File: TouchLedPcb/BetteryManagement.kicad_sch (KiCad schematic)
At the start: 1 part, among them U1 BQ25606

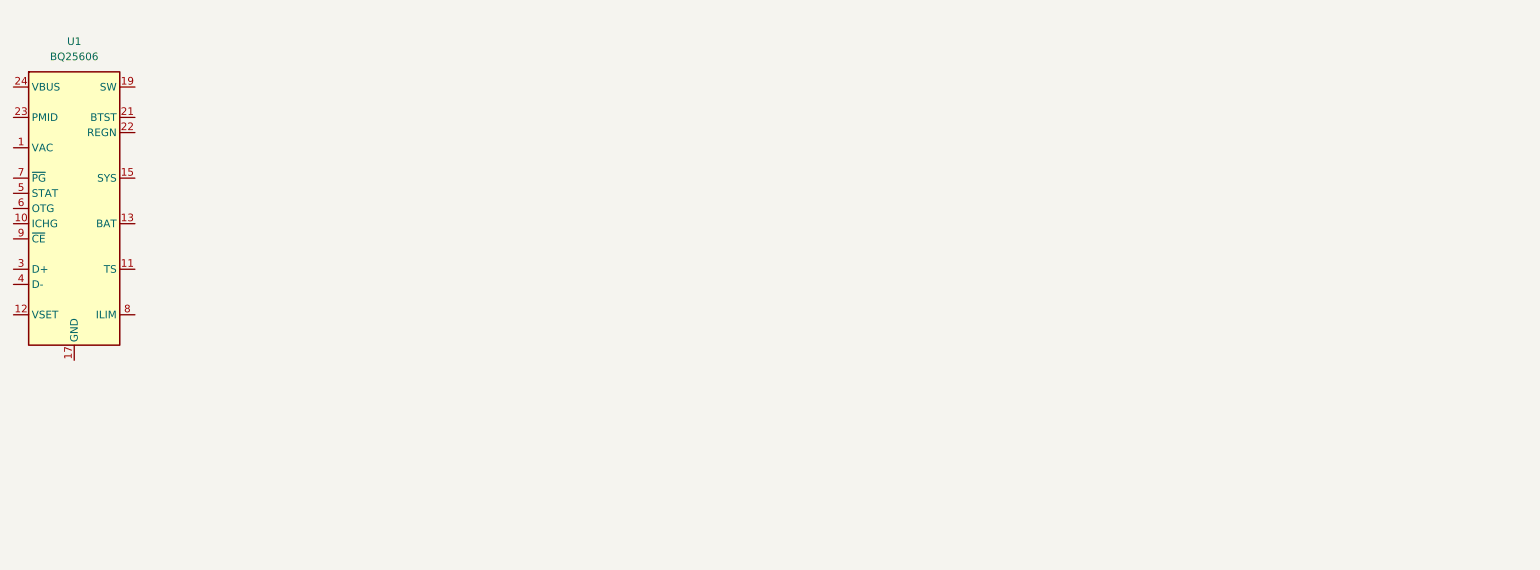
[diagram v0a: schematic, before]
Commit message: add excel for NTC 10k b=3950 calculation for BQ25606 -10~45C operation
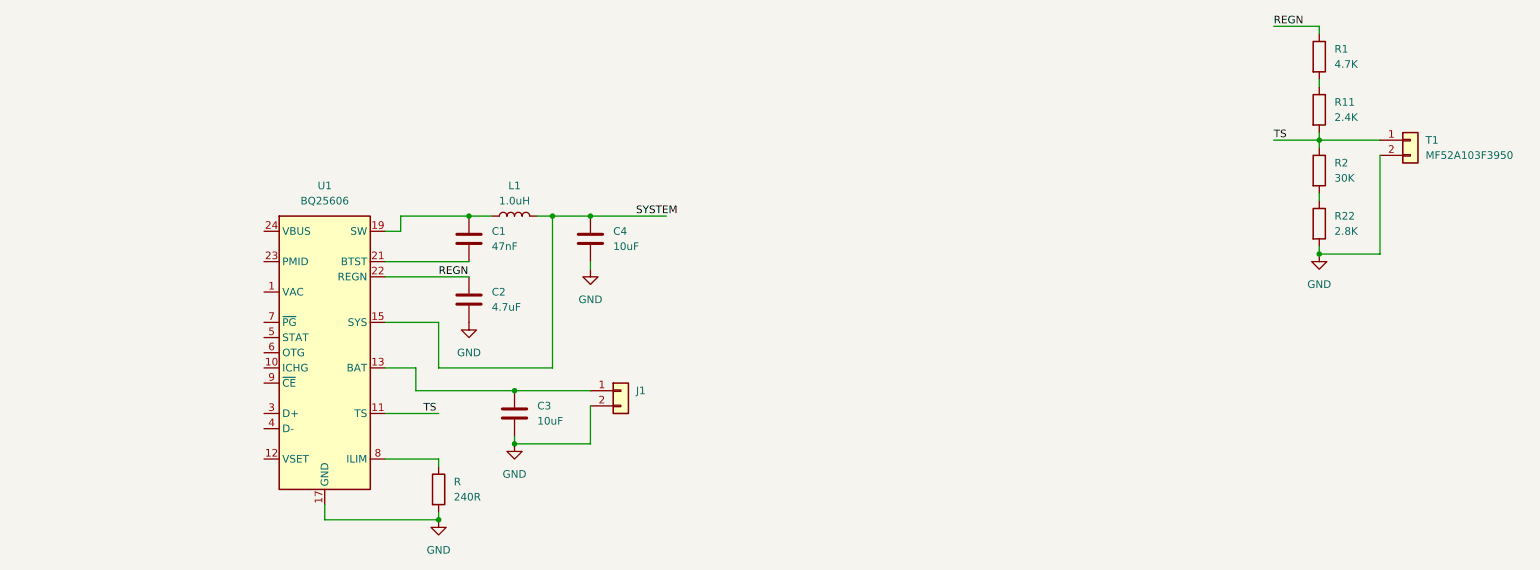
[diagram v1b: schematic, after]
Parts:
- added C1: 47nF, Capacitor_SMD:C_0805_2012Metric, symbol Device:C
- added C2: 4.7uF, Capacitor_SMD:C_1206_3216Metric, symbol Device:C
- added C3, C4: 10uF, Capacitor_SMD:C_0805_2012Metric, symbol Device:C
- added J1: ~, Connector_PinHeader_2.54mm:PinHeader_1x02_P2.54mm_Vertical, symbol Connector_Generic:Conn_01x02
- added L1: 1.0uH, Inductor_SMD:L_Chilisin_BMRA00050530, symbol Device:L
- added R: 240R, Resistor_SMD:R_0805_2012Metric, symbol Device:R
- added R1: 4.7K, Resistor_SMD:R_0805_2012Metric_Pad1.20x1.40mm_HandSolder, symbol Device:R
- added R11: 2.4K, Resistor_SMD:R_0805_2012Metric_Pad1.20x1.40mm_HandSolder, symbol Device:R
- added R2: 30K, Resistor_SMD:R_0805_2012Metric_Pad1.20x1.40mm_HandSolder, symbol Device:R
- added R22: 2.8K, Resistor_SMD:R_0805_2012Metric_Pad1.20x1.40mm_HandSolder, symbol Device:R
- added T1: MF52A103F3950, Connector_PinHeader_2.00mm:PinHeader_1x02_P2.00mm_Vertical, symbol Connector_Generic:Conn_01x02
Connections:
- net TS: now reaches U1.11 (TS)
- net TS: now also R11.2, R2.1, T1.1 (Pin_1)
- net at U1.13 (BAT), U1.14 (BAT): now also C3.1, J1.1 (Pin_1)
- net SYSTEM: now reaches U1.15 (SYS), U1.16 (SYS)
- net SYSTEM: now also C4.1, L1.2
- net GND: now reaches U1.17 (GND), U1.18 (GND), U1.25 (GND)
- net GND: now also C2.2, C3.2, C4.2, J1.2 (Pin_2), R.2, R22.2, T1.2 (Pin_2)
- net at U1.19 (SW), U1.20 (SW): now also C1.1, L1.1
- net at U1.21 (BTST): now also C1.2
- net REGN: now reaches U1.22 (REGN)
- net REGN: now also C2.1, R1.1
- net at U1.8 (ILIM): now also R.1
- new net: R2.2, R22.1
- new net: R1.2, R11.1
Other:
- moved on the sheet: U1
